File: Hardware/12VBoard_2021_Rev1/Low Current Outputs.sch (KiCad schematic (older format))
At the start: 53 parts, among them U14 LM2576S-12/NOPB, U2 INA198, U3 LM2576S-12/NOPB, U4 LM2576S-12/NOPB, U5 LM2576S-12/NOPB, U6 LM2576S-12/NOPB

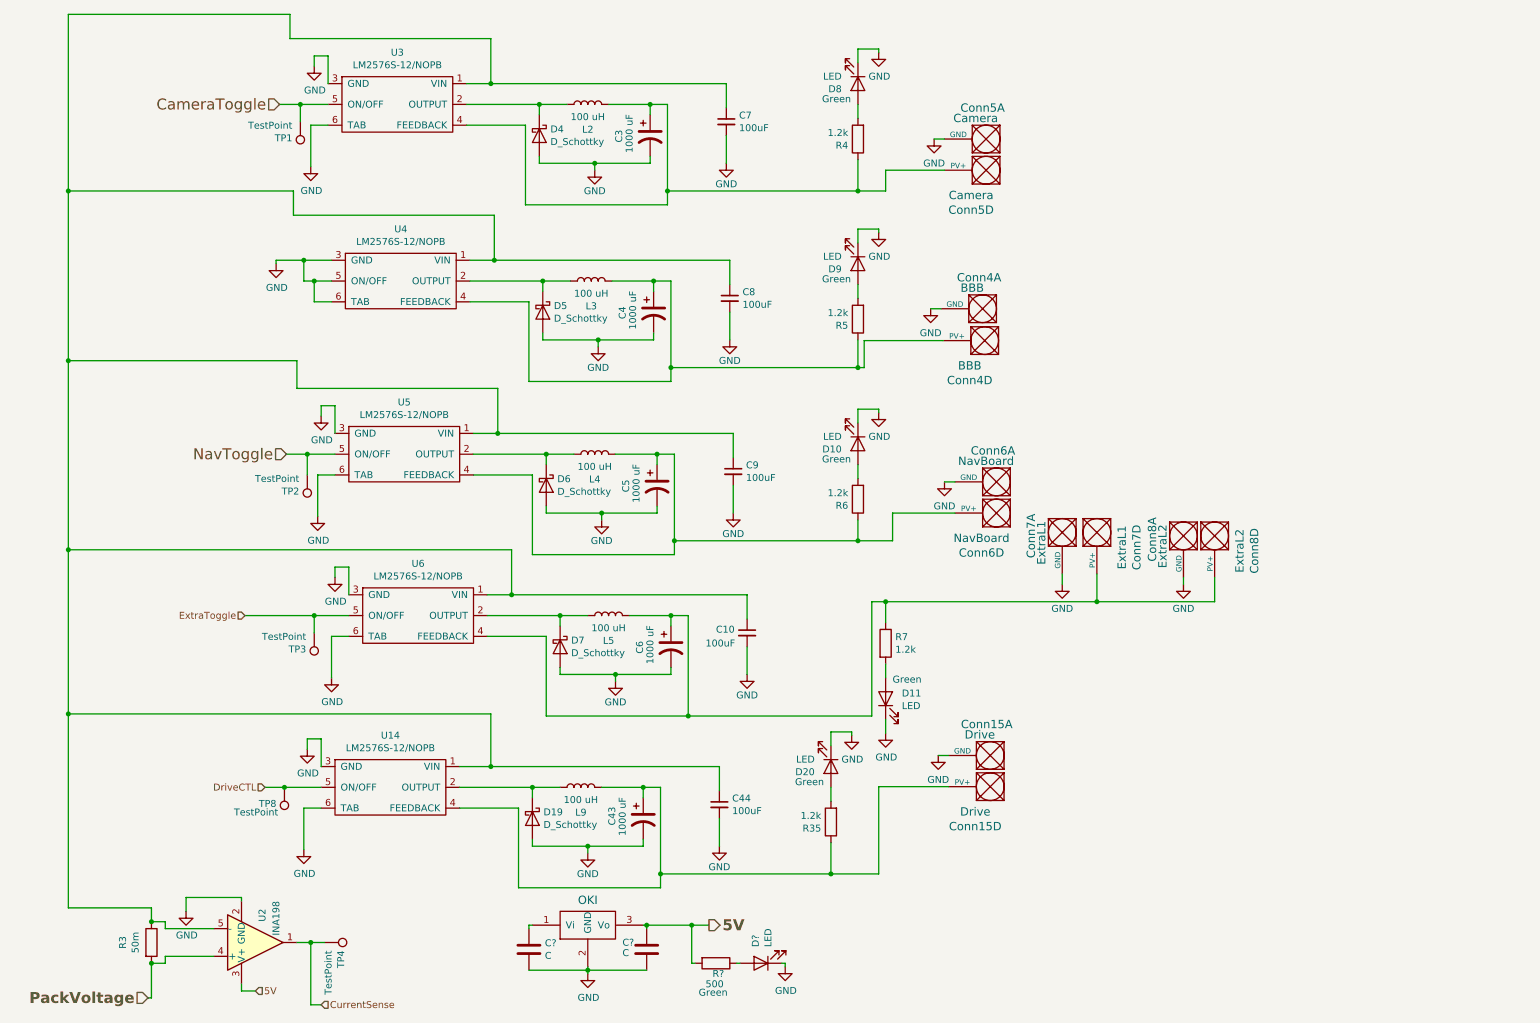
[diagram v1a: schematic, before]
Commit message: Added Mosfet cicuitry to turn on/off logic power for high current side
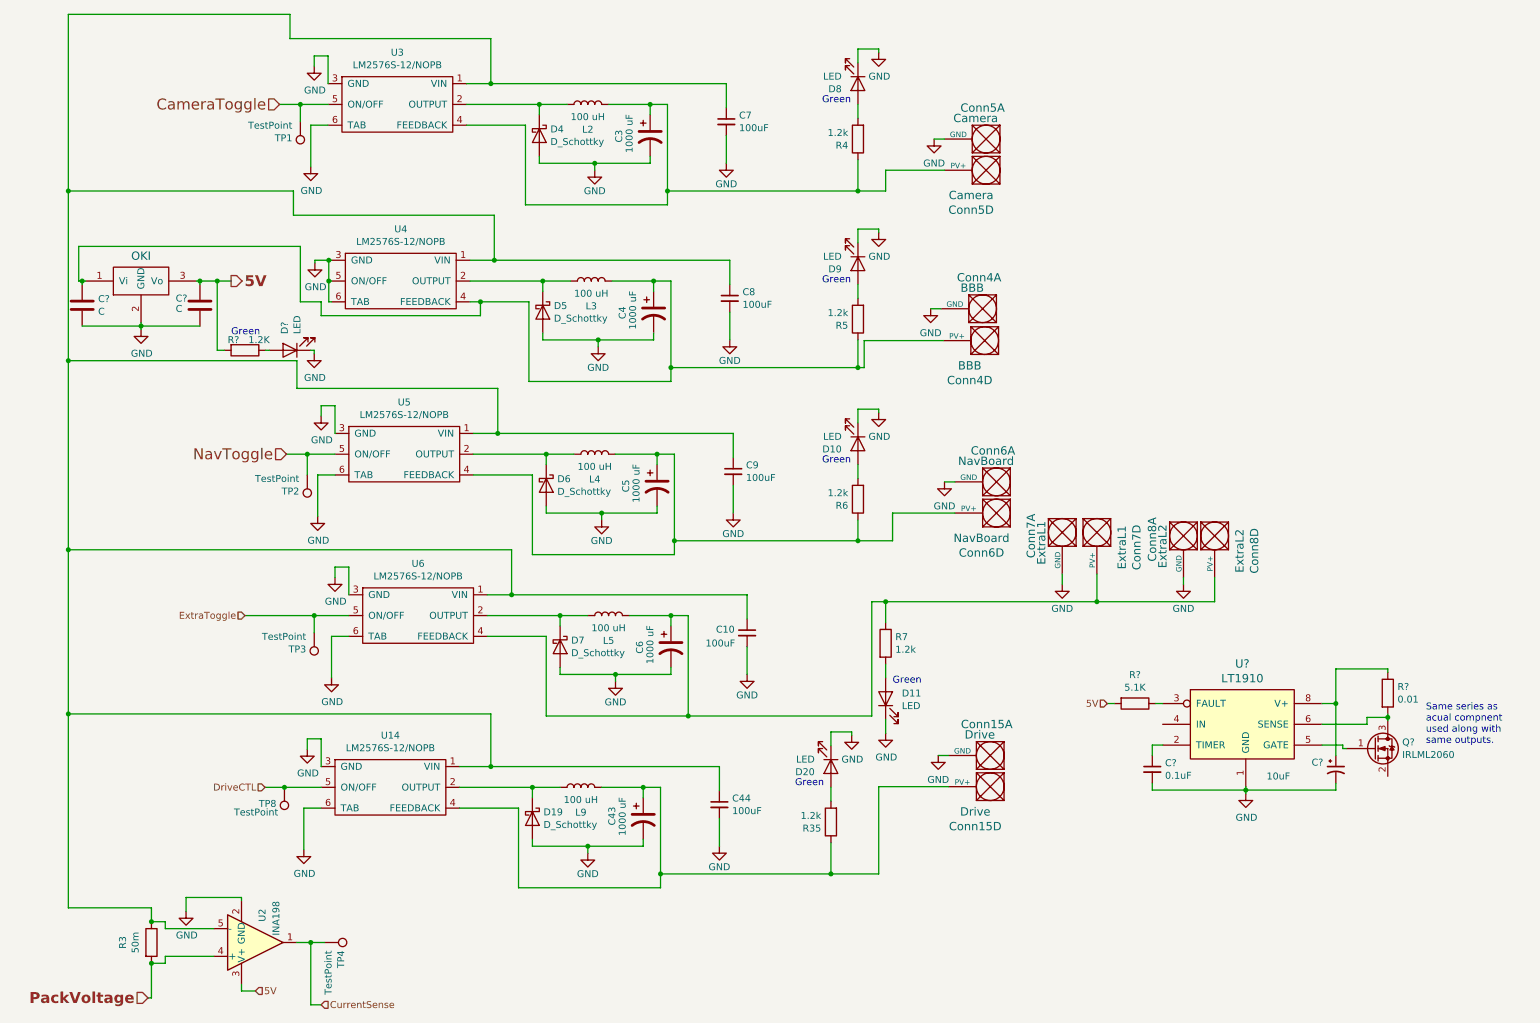
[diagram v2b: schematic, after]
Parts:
- added C?: 0.1uF, symbol Device:C_Small
- added C?: 10uF, symbol Device:CP1_Small
- added Q?: IRLML2060, Package_TO_SOT_SMD:SOT-23, symbol Transistor_FET:IRLML2060
- added R?: 0.01, symbol Device:R
- added R?: 5.1K, symbol Device:R
- added U?: LT1910, symbol MRDT_ICs:LT1910
- R?: value 500 -> 1.2K
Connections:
- net 5V: now also R?.2
- net GND: now also C?.2, C?.2, U?.1 (GND)
- net at C4.1, Conn4.4 (PV+), L3.2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: now also C?.1, U?.1 (Vi)
- new net: C?.1, U?.2 (TIMER)
- new net: R?.1, U?.3 (FAULT)
- new net: Q?.1 (G), U?.5 (GATE)
- new net: Q?.3 (D), R?.2, U?.6 (SENSE)
- new net: C?.1, R?.1, U?.8 (V+)
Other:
- note added: "Same series as \nacual compnent\nused along with\nsame outputs."
- moved on the sheet: C?, D?, R?

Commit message: Redesigned low current ports schematic
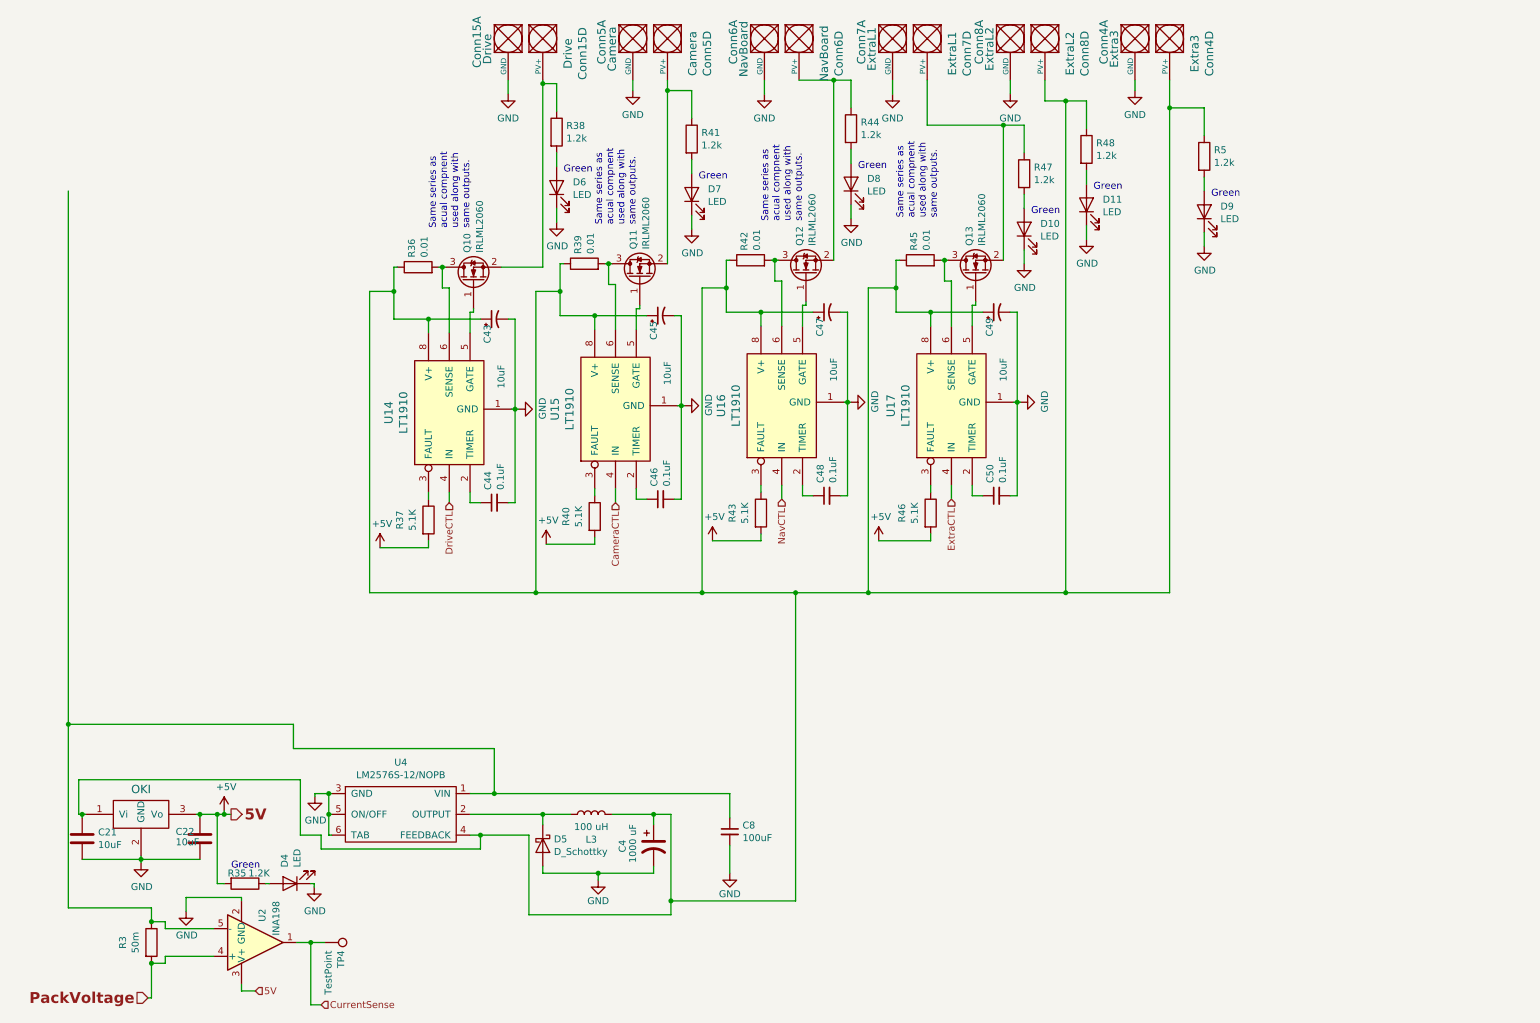
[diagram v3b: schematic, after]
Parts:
- removed C10, C7, C9: 100uF, Capacitor_SMD:C_0603_1608Metric_Pad1.05x0.95mm_HandSolder, symbol Device:C_Small
- removed C3, C43, C5, C6: 1000 uF, Capacitor_THT:CP_Radial_D10.0mm_P5.00mm, symbol Device:CP1
- removed D19, D4, D6, D7: D_Schottky, Diode_THT:D_DO-201AD_P15.24mm_Horizontal, symbol Device:D_Schottky
- removed D20: LED, Diode_SMD:D_0603_1608Metric_Pad1.05x0.95mm_HandSolder, symbol Device:LED
- removed L2, L4, L5, L9: 100 uH, Inductor_SMD:L_0603_1608Metric_Pad1.05x0.95mm_HandSolder, symbol Device:L
- removed R35, R4, R6, R7: 1.2k, Resistor_SMD:R_0603_1608Metric_Pad1.05x0.95mm_HandSolder, symbol Device:R
- removed TP1, TP2, TP3, TP8: TestPoint, TestPoint:TestPoint_Pad_2.5x2.5mm, symbol Connector:TestPoint
- removed U14, U3, U5, U6: LM2576S-12/NOPB, MRDT_Devices:LM2576, symbol 12VBoard_2021_Rev1-rescue:LM2576D2TR4-MRDT_Devices
- added C43, C45, C49: 10uF, symbol Device:CP1_Small
- added C46, C50: 0.1uF, symbol Device:C_Small
- added D6, D7: LED, Diode_SMD:D_0603_1608Metric_Pad1.05x0.95mm_HandSolder, symbol Device:LED
- added Q10, Q11, Q13: IRLML2060, Package_TO_SOT_SMD:SOT-23, symbol Transistor_FET:IRLML2060
- added R36, R39, R45: 0.01, symbol Device:R
- added R37, R40, R46: 5.1K, symbol Device:R
- added R38, R41, R44, R47, R48: 1.2k, Resistor_SMD:R_0603_1608Metric_Pad1.05x0.95mm_HandSolder, symbol Device:R
- added U14, U15, U17: LT1910, symbol MRDT_ICs:LT1910
- C21, C22: renamed from C?; value C -> 10uF; footprint (none) -> Capacitor_SMD:C_0603_1608Metric_Pad1.05x0.95mm_HandSolder
- C44: value 100uF -> 0.1uF; footprint Capacitor_SMD:C_0603_1608Metric_Pad1.05x0.95mm_HandSolder -> (none)
- Conn4: value BBB -> Extra3
- gave numbers to parts that had none: 9
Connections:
- net DriveCTL: now also U14.4 (IN)
- net GND: now also C43.2, C45.2, C46.2, C49.2, C50.2, D6.1 (K), D7.1 (K), U14.1 (GND), U15.1 (GND), U17.1 (GND)
- net at Conn5.4 (PV+): now also Q11.2 (S), R41.1
- net at C8.1, R3.1, U2.5 (-)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: no longer C44.1
- net at C21.1, C4.1, Conn4.4 (PV+)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: now also C47.1, Conn8.4 (PV+), R42.1, U16.8 (V+), C43.1, C45.1, C49.1, R36.1, R39.1, R45.1, R48.1, U14.8 (V+), U15.8 (V+), U17.8 (V+)
- net at Conn6.4 (PV+): now also Q12.2 (S), R44.1
- net at Conn7.4 (PV+): now also Q13.2 (S), R47.1; no longer Conn8.4 (PV+)
- net at D11.2 (A): now also R48.2
- net at D10.2 (A): now also R47.2
- net at D8.2 (A): now also R44.2
- net at Conn15.4 (PV+): now also Q10.2 (S), R38.1
- net NavCTL: now reaches U16.4 (IN)
- net 5V renamed +5V
- net +5V: now also R37.2, R40.2, R46.2
- new net: C44.1, U14.2 (TIMER)
- new net: R37.1, U14.3 (FAULT)
- new net: Q10.1 (G), U14.5 (GATE)
- new net: Q10.3 (D), R36.2, U14.6 (SENSE)
- new net: C46.1, U15.2 (TIMER)
- new net: R40.1, U15.3 (FAULT)
- new net: Q11.1 (G), U15.5 (GATE)
- new net: Q11.3 (D), R39.2, U15.6 (SENSE)
- new net: C50.1, U17.2 (TIMER)
- new net: R46.1, U17.3 (FAULT)
- new net: Q13.1 (G), U17.5 (GATE)
- new net: Q13.3 (D), R45.2, U17.6 (SENSE)
- new net: D7.2 (A), R41.2
- new net: D6.2 (A), R38.2
- new net CameraCTL: U15.4 (IN)
- new net ExtraCTL: U17.4 (IN)
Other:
- moved on the sheet: C21, C22, C4, C47, C48, C8, Conn15A, Conn15D, Conn4A, Conn4D, Conn5A, Conn5D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

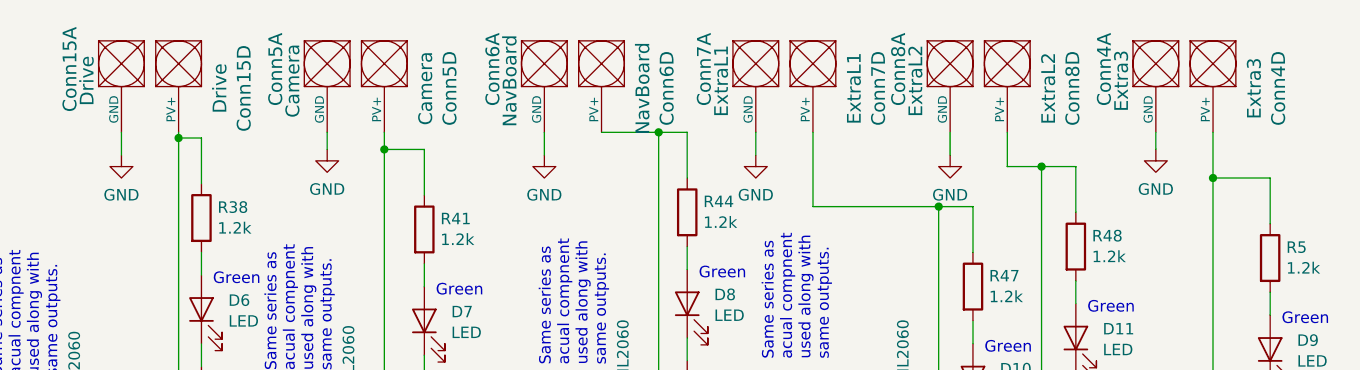
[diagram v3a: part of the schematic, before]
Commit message: Layed out logic power
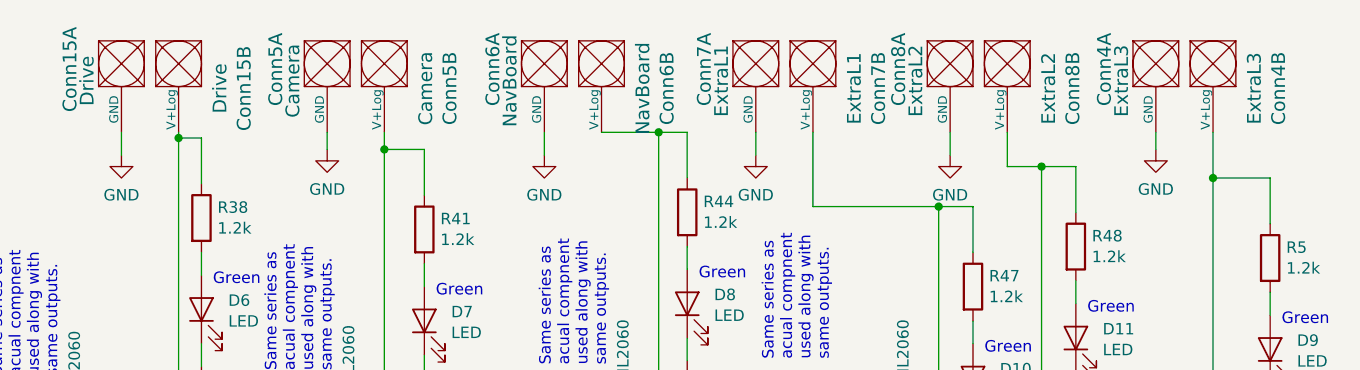
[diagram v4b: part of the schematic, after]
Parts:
- C4: footprint Capacitor_THT:CP_Radial_D10.0mm_P5.00mm -> Capacitor_THT:CP_Radial_D12.5mm_P5.00mm
- C43, C45, C47, C49: footprint (none) -> Capacitor_THT:CP_Radial_D5.0mm_P2.00mm
- C44, C46, C48, C50: footprint (none) -> Capacitor_SMD:C_0603_1608Metric_Pad1.05x0.95mm_HandSolder
- Conn15, Conn5, Conn6, Conn7, Conn8: footprint MRDT_Connectors:Anderson_2_Horizontal_Stacked -> MRDT_Connectors:Anderson_2_Vertical_Sidy_by_Side
- Conn4: value Extra3 -> ExtraL3; footprint MRDT_Connectors:Anderson_2_Horizontal_Stacked -> MRDT_Connectors:Anderson_2_Vertical_Sidy_by_Side
- D5: footprint Diode_THT:D_DO-201AD_P15.24mm_Horizontal -> Diode_THT:D_DO-201AD_P5.08mm_Vertical_KathodeUp
- R36, R37, R39, R40, R42, R43, R45, R46: footprint (none) -> Resistor_SMD:R_0603_1608Metric_Pad1.05x0.95mm_HandSolder
- U14, U15, U16, U17: footprint (none) -> Package_SO:SOIC-8-N7_3.9x4.9mm_P1.27mm
- U9: footprint (none) -> MRDT_Devices:OKI_Horizontal
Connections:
- net at C21.1, C4.1, C43.1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: now also Conn4.2 (V+Log), Conn8.2 (V+Log); no longer Conn4.4 (PV+), Conn8.4 (PV+)
- net at Q13.2 (S), R47.1: now also Conn7.2 (V+Log); no longer Conn7.4 (PV+)
- net at Q11.2 (S), R41.1: now also Conn5.2 (V+Log); no longer Conn5.4 (PV+)
- net at Q12.2 (S), R44.1: now also Conn6.2 (V+Log); no longer Conn6.4 (PV+)
- net at Q10.2 (S), R38.1: now also Conn15.2 (V+Log); no longer Conn15.4 (PV+)

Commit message: found Big inductors
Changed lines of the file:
@@
 Wire Wire Line
 	725  5700 2350 5700
-Wire Wire Line
-	725  1850 725  5700
 $Comp
 L power:GND #PWR?
@@
 Wire Wire Line
 	6675 1050 6675 1150
-Connection ~ 725  5700
 Wire Wire Line
 	725  5700 725  7025

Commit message: Added all logic circuits for high current
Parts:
- R3: footprint Resistor_SMD:R_2512_6332Metric_Pad1.52x3.35mm_HandSolder -> Package_TO_SOT_THT:TO-126-2_Vertical
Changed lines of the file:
@@
 F 0 "R3" V 1118 7275 50  0000 C CNN
 F 1 "50m" V 1209 7275 50  0000 C CNN
-F 2 "Resistor_SMD:R_2512_6332Metric_Pad1.52x3.35mm_HandSolder" V 1255 7275 50  0001 C CNN
+F 2 "Package_TO_SOT_THT:TO-126-2_Vertical" V 1255 7275 50  0001 C CNN
 F 3 "~" H 1325 7275 50  0001 C CNN
 	1    1325 7275
